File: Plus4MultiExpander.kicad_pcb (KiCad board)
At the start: 2 copper layers, 62.2 x 99.9 mm, 17 parts, among them CN1 EDGE_CONN, CN2 C16_NEWSTYLE_EXP_PORT_1, CN3 C16_NEWSTYLE_EXP_PORT_2, CN4 C16_NEWSTYLE_EXP_PORT_3, U1 74HCT245, U2 74HCT245, U3 74HCT08

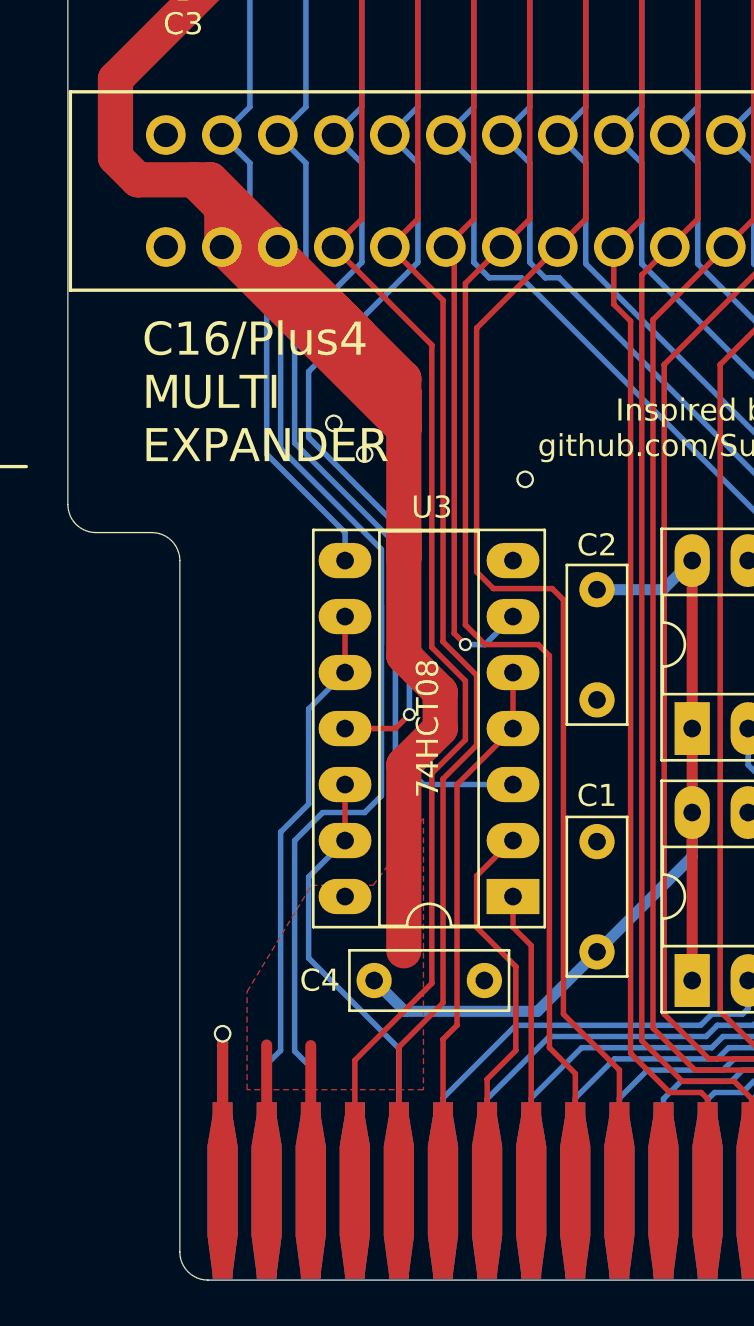
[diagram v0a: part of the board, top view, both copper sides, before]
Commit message: Buffer R/W instead of PHI0
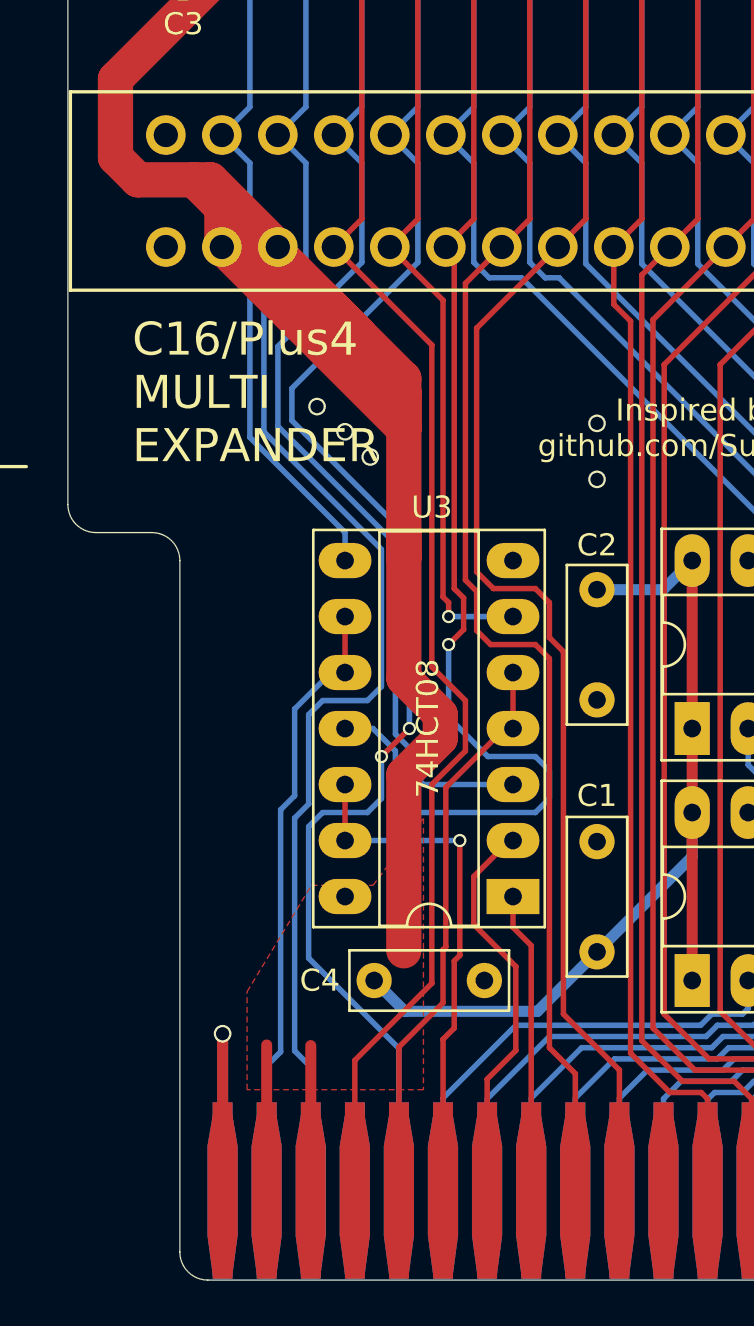
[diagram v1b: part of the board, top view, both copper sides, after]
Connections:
- CN1 pad 5: /r_~w -> /r_~w~_in
- CN1 pad E: /phi0_in -> /phi0
- U3 pad 11: /phi0 -> /~c1hi
- U3 pad 12: /phi0_in -> /~c1hi_in
- U3 pad 13: /phi0_in -> /~c1hi_in
- U3 pad 4: /~c1hi_in -> /r_~w~_in
- U3 pad 5: /~c1hi_in -> /r_~w~_in
- U3 pad 6: /~c1hi -> /r_~w
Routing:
- net /r_~w~_in: track 0.00 -> 25.9 mm
- net /r_~w: track 94.0 -> 68.9 mm, vias 0 -> 1
- net /phi0: track 82.0 -> 105.8 mm, vias 1 -> 2
- net /phi0_in: track 20.8 -> 0.00 mm
- net /~c1hi: track 69.2 -> 89.0 mm
- net /~reset: track 103.7 -> 102.6 mm
- net /~c1hi_in: track 24.8 -> 23.9 mm, vias 0 -> 1
- net /~c2: track 85.8 -> 86.4 mm
- net GND: vias 5 -> 7

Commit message: Better routing
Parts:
- C3: footprint Capacitor_THT:CP_Radial_D8.0mm_P3.50mm -> Plus4MultiExpander:CP_Radial_L11.5mm_D8.0mm_P3.5mm_Horizontal
- moved C3 2.66 mm to (125.6, 85.1), turned to 0 degrees
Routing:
- net +5V: track 255.4 -> 277.0 mm
- net /~c1hi: track 89.0 -> 74.3 mm
- net /phi0: track 105.8 -> 109.5 mm
- net /~c2: track 86.4 -> 84.1 mm
- net /~irq: track 95.4 -> 93.7 mm
- net /~c1hi_in: track 23.9 -> 23.2 mm
- net GND: vias 7 -> 6

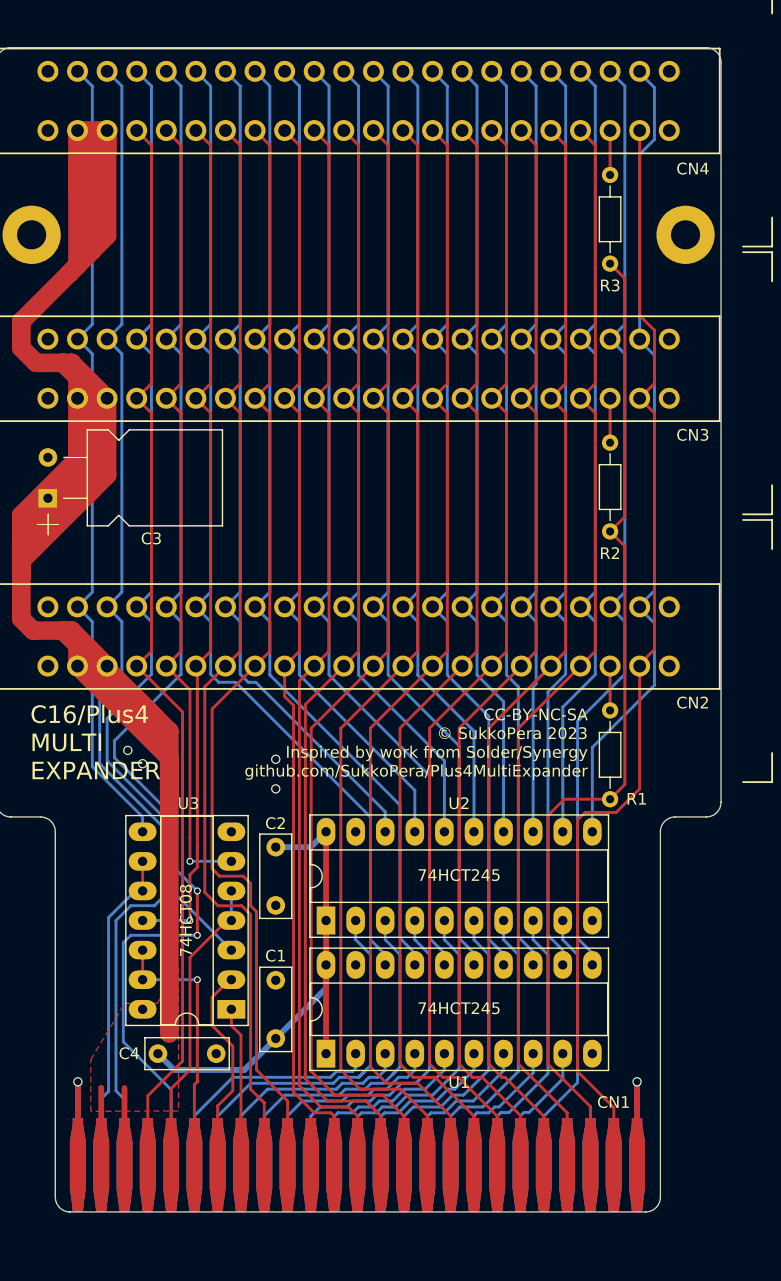
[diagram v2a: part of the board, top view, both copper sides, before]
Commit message: New pin mapping
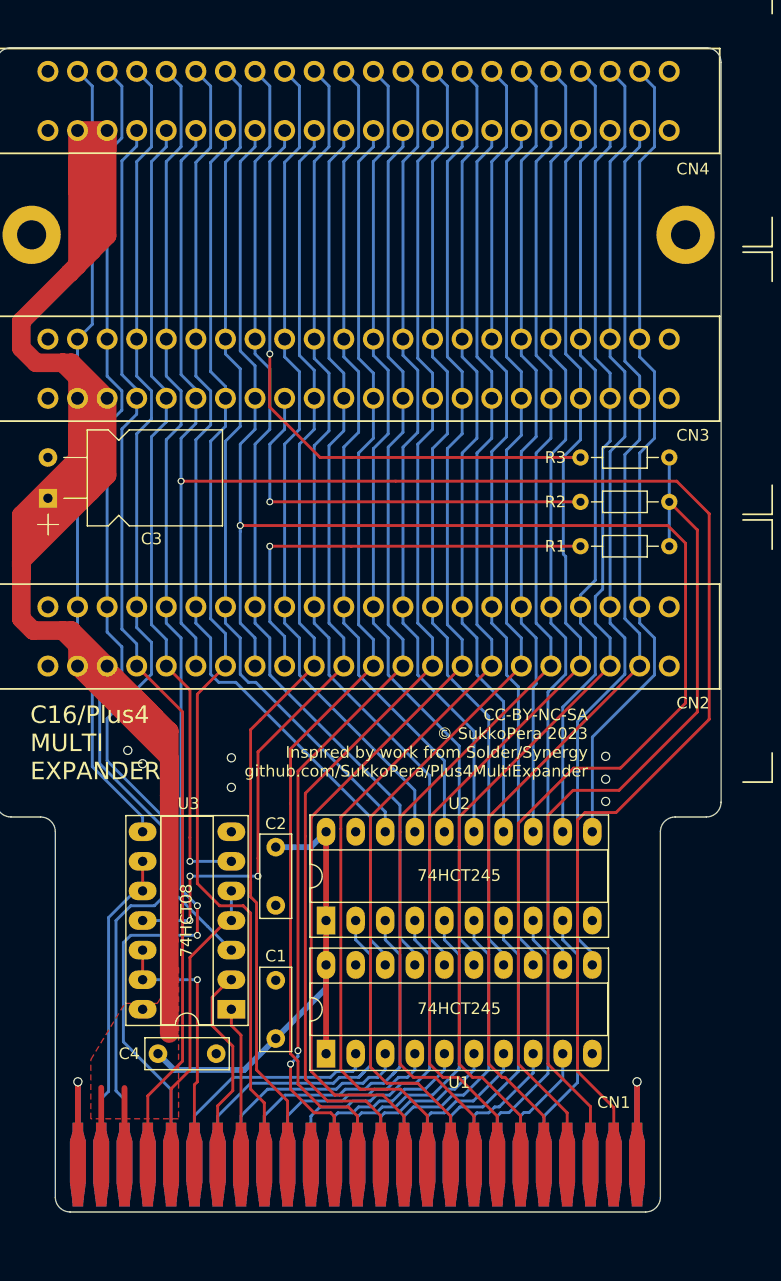
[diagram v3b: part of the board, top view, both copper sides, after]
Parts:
- moved R3 24.4 mm to (171.3, 83.3), turned to 0 degrees
- moved R1 14.3 mm to (171.3, 90.9), turned to 0 degrees
- moved R2 5.68 mm to (171.3, 87.1), turned to 0 degrees
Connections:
- CN2 pad 10: /ba -> /~cs0
- CN2 pad 11: /d7 -> /~c1hi
- CN2 pad 12: /d6 -> /ba
- CN2 pad 13: /d5 -> /mux
- CN2 pad 14: /d4 -> /d7
- CN2 pad 15: /d3 -> /d6
- CN2 pad 16: /d2 -> /d5
- CN2 pad 17: /d1 -> /d4
- CN2 pad 18: /d0 -> /d3
- CN2 pad 19: /aec -> /d2
- CN2 pad 20: Net-(CN2-Pad20) -> /d1
- CN2 pad 21: /phi2 -> /d0
- CN2 pad 6: /~c1hi -> /phi2
- CN2 pad 8: /~cs0 -> /aec
- CN2 pad 9: /mux -> Net-(CN2-Pad9)
- CN3 pad 10: /ba -> /~cs0
- CN3 pad 11: /d7 -> /~c1hi
- CN3 pad 12: /d6 -> /ba
- CN3 pad 13: /d5 -> /mux
- CN3 pad 14: /d4 -> /d7
- CN3 pad 15: /d3 -> /d6
- CN3 pad 16: /d2 -> /d5
- CN3 pad 17: /d1 -> /d4
- CN3 pad 18: /d0 -> /d3
- CN3 pad 19: /aec -> /d2
- CN3 pad 20: Net-(CN3-Pad20) -> /d1
- CN3 pad 21: /phi2 -> /d0
- CN3 pad 6: /~c1hi -> /phi2
- CN3 pad 8: /~cs0 -> /aec
- CN3 pad 9: /mux -> Net-(CN3-Pad9)
- CN4 pad 10: /ba -> /~cs0
- CN4 pad 11: /d7 -> /~c1hi
- CN4 pad 12: /d6 -> /ba
- CN4 pad 13: /d5 -> /mux
- CN4 pad 14: /d4 -> /d7
- CN4 pad 15: /d3 -> /d6
- CN4 pad 16: /d2 -> /d5
- CN4 pad 17: /d1 -> /d4
- CN4 pad 18: /d0 -> /d3
- CN4 pad 19: /aec -> /d2
- CN4 pad 20: Net-(CN4-Pad20) -> /d1
- CN4 pad 21: /phi2 -> /d0
- CN4 pad 6: /~c1hi -> /phi2
- CN4 pad 8: /~cs0 -> /aec
- CN4 pad 9: /mux -> Net-(CN4-Pad9)
- R1 pad 1: Net-(CN2-Pad20) -> Net-(CN2-Pad9)
- R2 pad 1: Net-(CN3-Pad20) -> Net-(CN3-Pad9)
- R3 pad 1: Net-(CN4-Pad20) -> Net-(CN4-Pad9)
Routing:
- net /phi2: track 95.9 -> 158.0 mm, vias 0 -> 1
- net /aec: track 94.8 -> 150.3 mm, vias 0 -> 1
- net Net-(CN4-Pad9): track 0.00 -> 52.7 mm, vias 0 -> 1
- net Net-(CN2-Pad9): track 0.00 -> 37.5 mm, vias 0 -> 1
- net Net-(CN3-Pad9): track 0.00 -> 36.1 mm, vias 0 -> 1
- net /ext_audio: track 85.5 -> 74.6 mm
- net /~c1hi: track 74.3 -> 82.9 mm, vias 1 -> 3
- net /phi0: track 109.5 -> 104.7 mm
- net Net-(CN4-Pad20): track 3.81 -> 0.00 mm
- net Net-(CN3-Pad20): track 3.81 -> 0.00 mm
- net Net-(CN2-Pad20): track 3.81 -> 0.00 mm
- net /mux: track 93.5 -> 97.3 mm, vias 0 -> 2
- net /ba: track 94.8 -> 98.6 mm
- net /d2: track 96.3 -> 99.6 mm
- net /d6: track 98.8 -> 102.0 mm
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
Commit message: Refinements
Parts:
- moved V0 8.63 mm to (160.9, 109.6)
- moved C1 0.13 mm to (145.0, 133.2)
- moved C2 0.13 mm to (145.0, 116.8)
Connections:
- U3 pad 11: /~c1hi -> /r_~w
- U3 pad 12: /~c1hi_in -> /r_~w~_in
- U3 pad 13: /~c1hi_in -> /r_~w~_in
- U3 pad 4: /r_~w~_in -> /~c1hi_in
- U3 pad 5: /r_~w~_in -> /~c1hi_in
- U3 pad 6: /r_~w -> /~c1hi
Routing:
- net /~c1hi: track 82.9 -> 74.2 mm, vias 3 -> 0
- net /~cs0: track 95.3 -> 102.3 mm
- net /r_~w: track 69.2 -> 74.8 mm
- net /phi0: track 104.7 -> 109.5 mm
- net /~c1lo: track 72.6 -> 69.7 mm
- net /r_~w~_in: track 25.9 -> 23.1 mm, vias 0 -> 1
- net /~c1hi_in: track 23.2 -> 25.2 mm, vias 1 -> 0
- net /ba: track 98.6 -> 97.7 mm
- net GND: vias 9 -> 11

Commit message: Final touches
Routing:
- net +5V: track 276.9 -> 275.7 mm

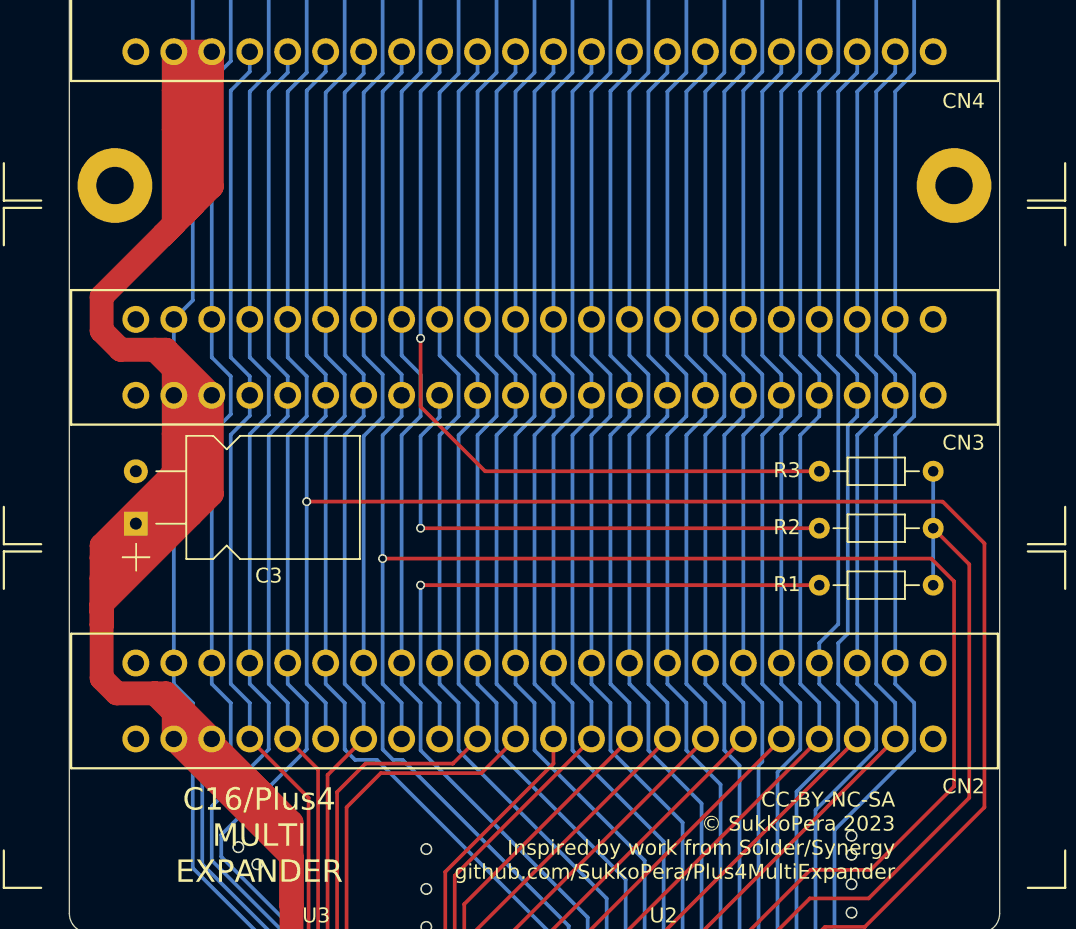
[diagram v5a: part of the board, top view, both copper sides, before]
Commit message: Active mixer prototype
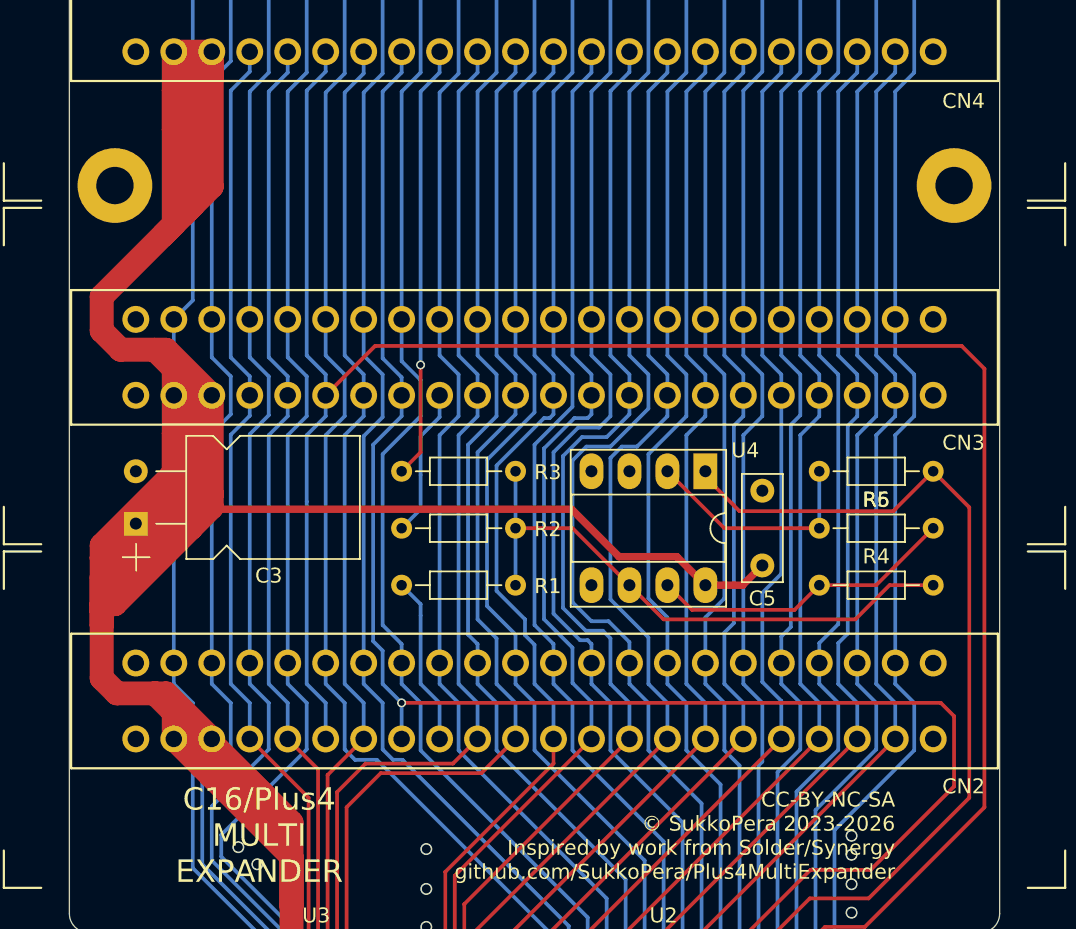
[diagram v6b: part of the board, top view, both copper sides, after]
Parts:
- added C5: 100n, Capacitor_THT:C_Disc_D7.0mm_W2.5mm_P5.00mm, F.Cu at (167.5, 89.6)
- added R4: 1k, Resistor_THT:R_Axial_DIN0204_L3.6mm_D1.6mm_P7.62mm_Horizontal, F.Cu at (171.3, 90.9)
- added R5: 1k, Resistor_THT:R_Axial_DIN0204_L3.6mm_D1.6mm_P7.62mm_Horizontal, F.Cu at (171.3, 87.1)
- added R6: 1k, Resistor_THT:R_Axial_DIN0204_L3.6mm_D1.6mm_P7.62mm_Horizontal, F.Cu at (178.9, 83.3)
- added U4: TLC272, Package_DIP:DIP-8_W7.62mm_Socket_LongPads, F.Cu at (163.7, 83.3)
- moved R1 20.3 mm to (151.0, 90.9), turned to 180 degrees
- moved R2 20.3 mm to (151.0, 87.1), turned to 180 degrees
- moved R3 20.3 mm to (151.0, 83.3), turned to 180 degrees
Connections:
- CN2 pad 9: Net-(CN2-Pad9) -> /ext_audio1
- CN3 pad 9: Net-(CN3-Pad9) -> /ext_audio2
- CN4 pad 9: Net-(CN4-Pad9) -> /ext_audio3
- R1 pad 1: Net-(CN2-Pad9) -> Net-(R1-Pad1)
- R1 pad 2: /ext_audio -> /ext_audio1
- R2 pad 1: Net-(CN3-Pad9) -> Net-(R1-Pad1)
- R2 pad 2: /ext_audio -> /ext_audio2
- R3 pad 1: Net-(CN4-Pad9) -> Net-(R1-Pad1)
- R3 pad 2: /ext_audio -> /ext_audio3
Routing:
- net +5V: track 275.7 -> 331.0 mm
- net Net-(CN4-Pad9): track 52.7 -> 0.00 mm, vias 1 -> 0
- net Net-(R1-Pad1): track 0.00 -> 39.0 mm
- net Net-(CN2-Pad9): track 37.5 -> 0.00 mm, vias 1 -> 0
- net Net-(CN3-Pad9): track 36.1 -> 0.00 mm, vias 1 -> 0
- net /ext_audio3: track 0.00 -> 29.1 mm, vias 0 -> 1
- net Net-(R4-Pad1): track 0.00 -> 20.7 mm
- net Net-(R5-Pad1): track 0.00 -> 15.5 mm
- net /ext_audio: track 74.6 -> 88.5 mm
- net /ext_audio1: track 0.00 -> 11.3 mm
- net /phi2: track 158.0 -> 169.2 mm, vias 1 -> 0
- net /aec: track 150.3 -> 140.3 mm
- net /ext_audio2: track 0.00 -> 9.94 mm
- net /ba7: track 81.3 -> 86.1 mm
- net /d7: track 100.1 -> 104.4 mm
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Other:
- board text added: "CC-BY-NC-SA © SukkoPera 2023-2026 Inspired by work from Solder/Synergy github.com/SukkoPera/Plus4MultiExpander"
- board text added: "V2"
- board text removed: "CC-BY-NC-SA © SukkoPera 2023 Inspired by work from Solder/Synergy github.com/SukkoPera/Plus4MultiExpander"
- board text removed: "V1"
